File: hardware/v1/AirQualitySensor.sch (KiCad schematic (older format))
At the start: 40 parts, among them J1 USB_C_Receptacle_USB2.0, J2 SWD, J3 UART, U1 004-0-0053, U2 DHT22, U3 XC6206P332MR

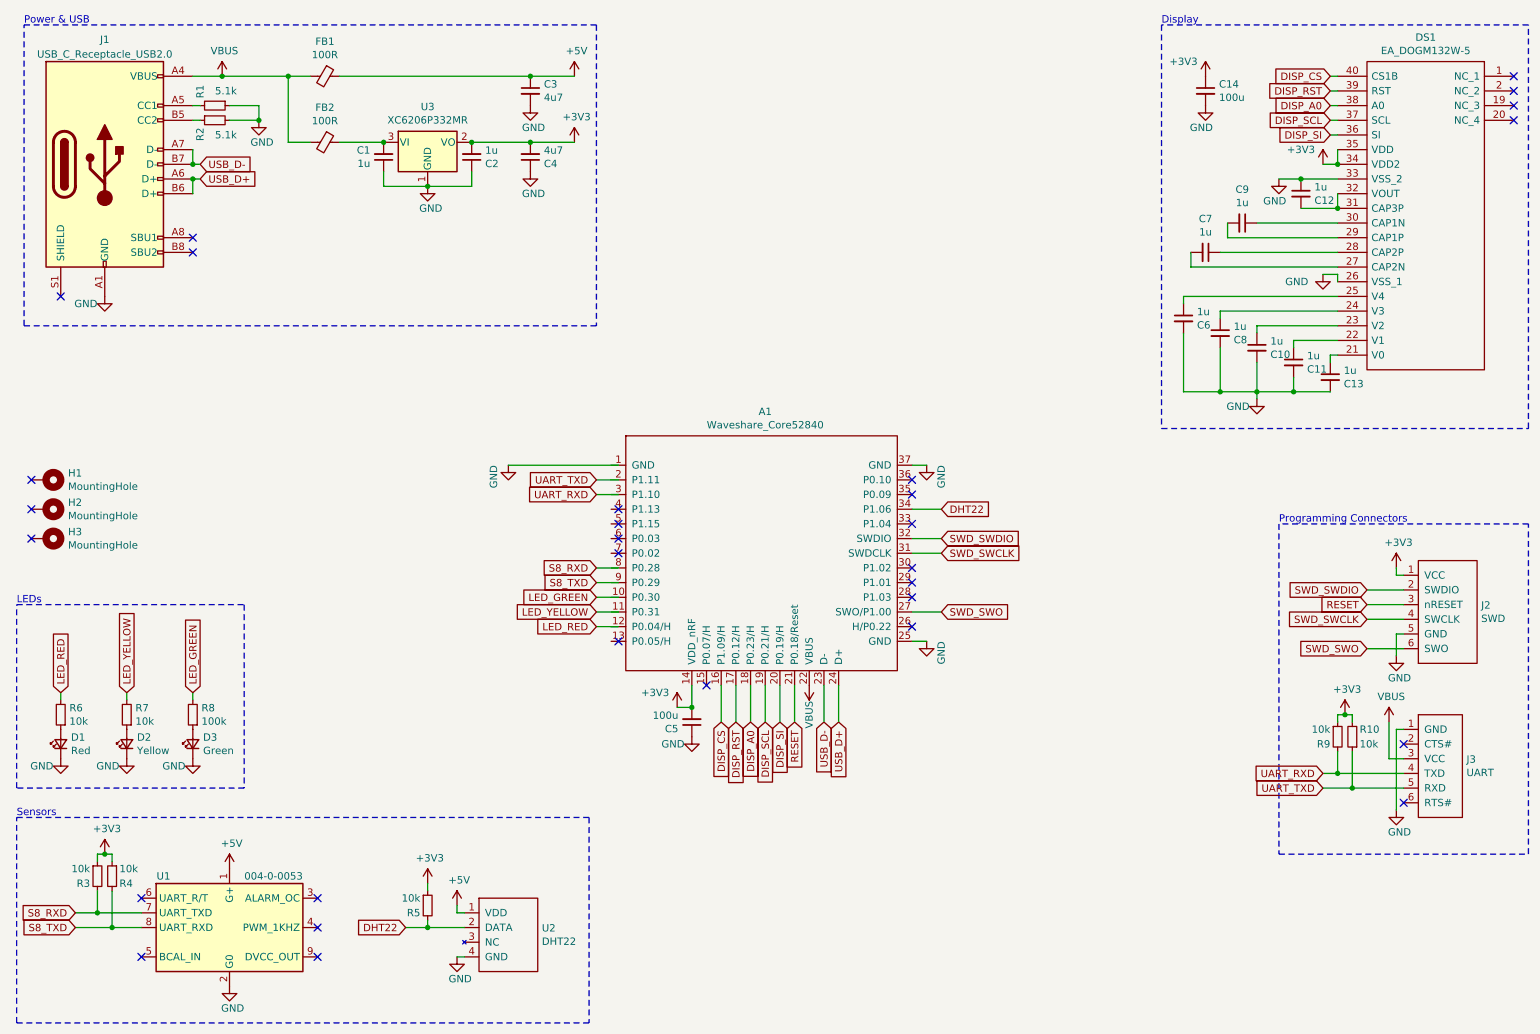
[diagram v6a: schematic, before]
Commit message: Move sensor pins to high drive output pins
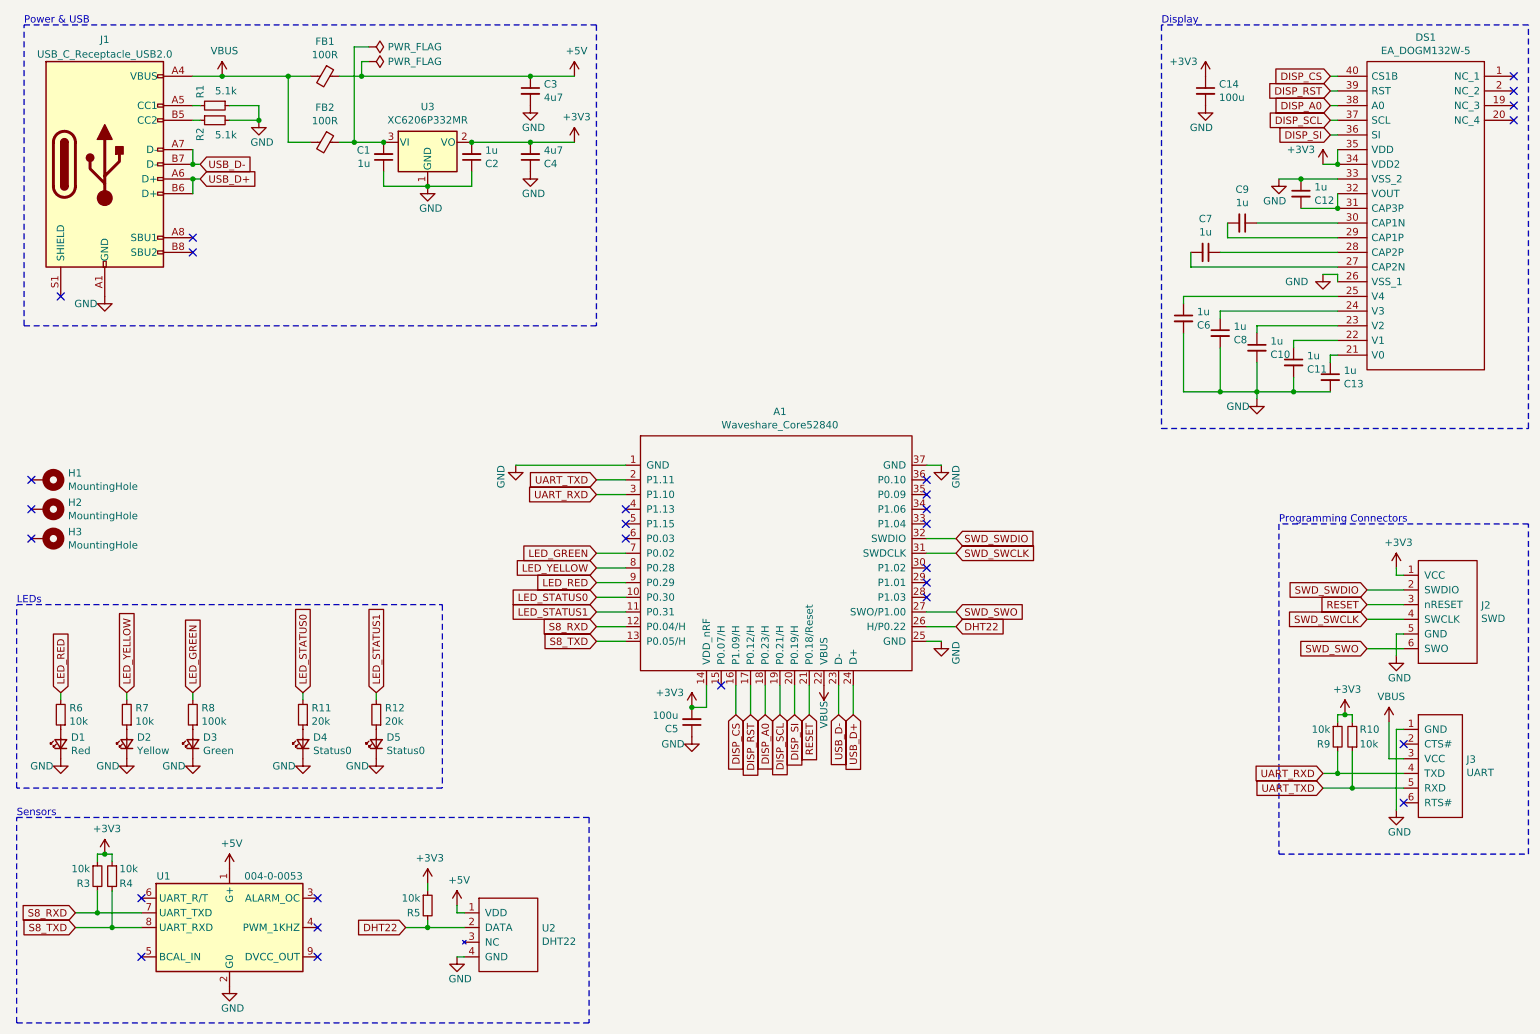
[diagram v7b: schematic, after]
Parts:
- added D4, D5: Status0, LED_SMD:LED_0805_2012Metric, symbol Device:LED_Small
- added R11, R12: 20k, Resistor_SMD:R_0402_1005Metric, symbol Device:R_Small
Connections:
- net labels added: LED_STATUS0, LED_STATUS1
- wire segments 127 -> 137
- no-connect marks 30 -> 28
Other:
- moved on the sheet: A1

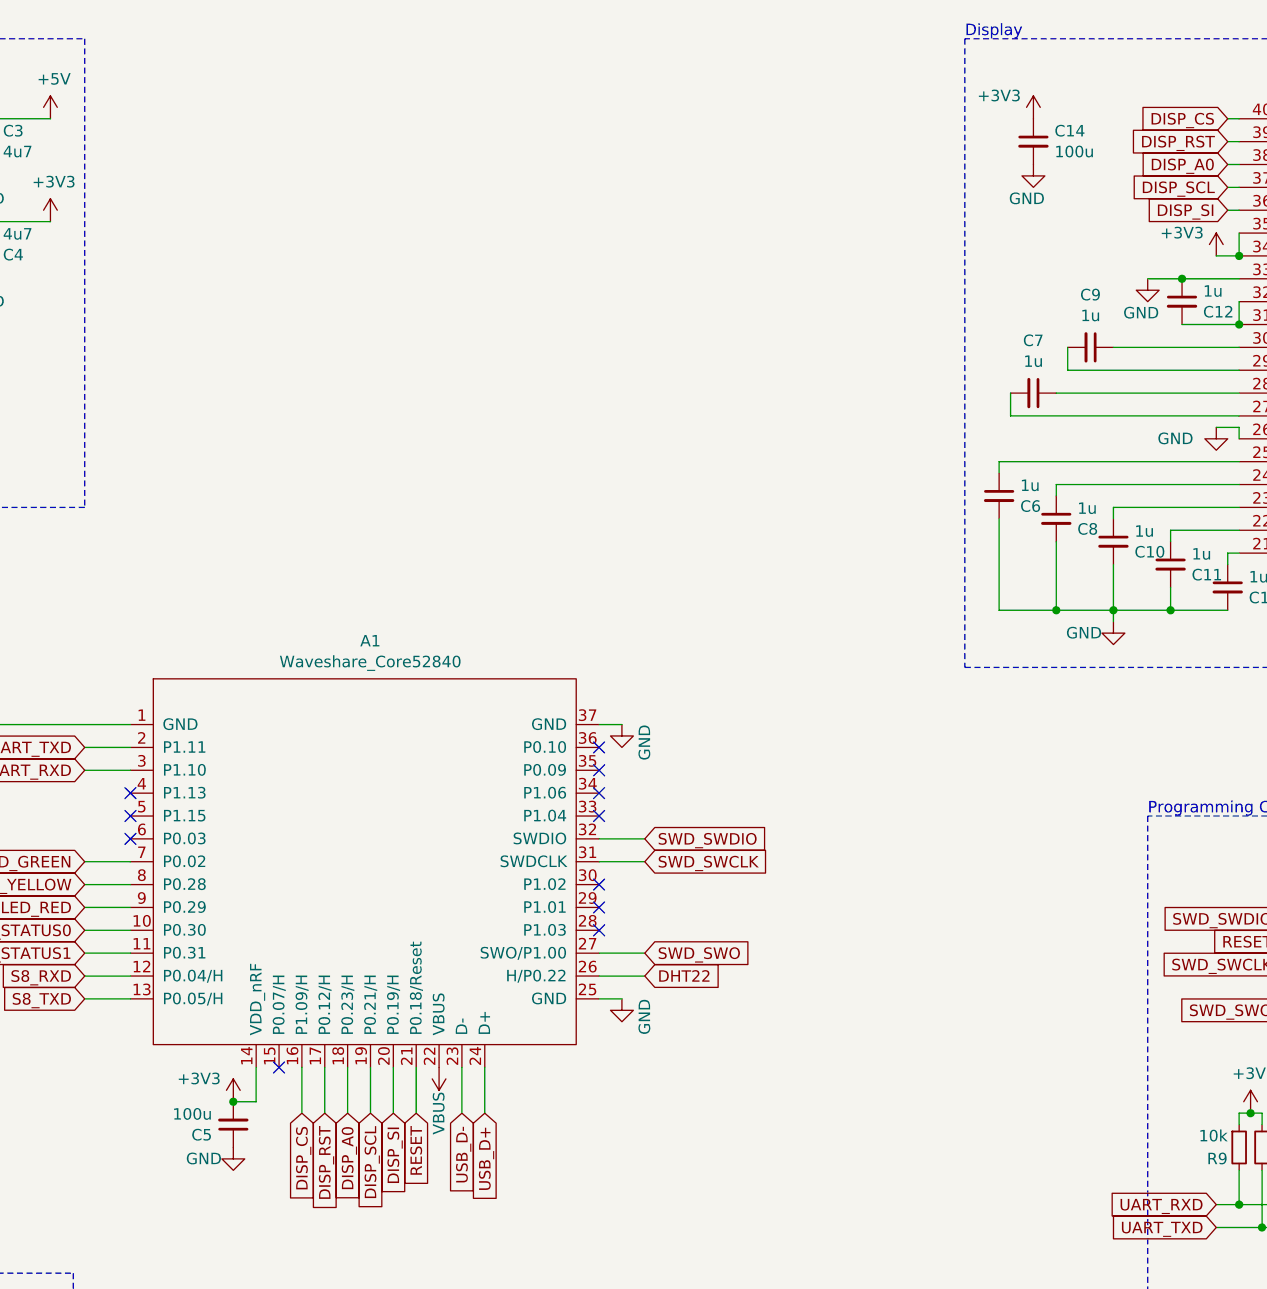
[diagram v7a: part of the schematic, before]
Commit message: Fix 100n capacitor values typo
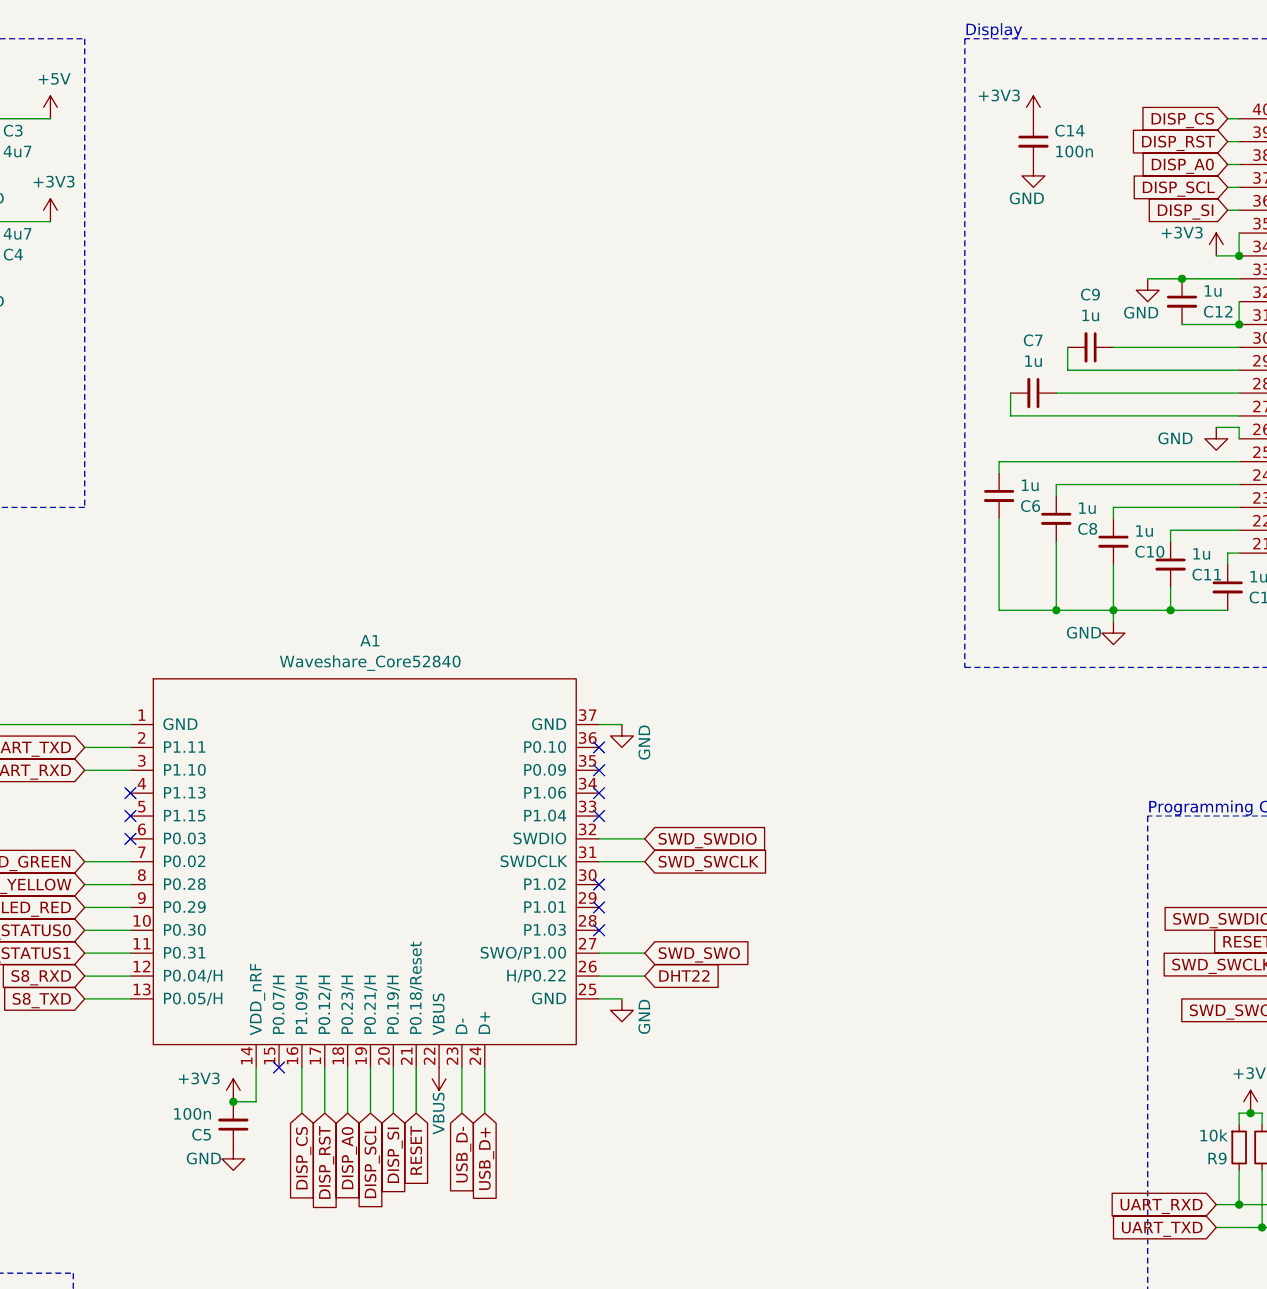
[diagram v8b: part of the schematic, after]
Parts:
- C14, C5: value 100u -> 100n
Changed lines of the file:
@@
 P 5350 5450
 F 0 "C5" H 5442 5496 50  0000 L CNN
-F 1 "100u" H 5442 5405 50  0000 L CNN
+F 1 "100n" H 5442 5405 50  0000 L CNN
 F 2 "Capacitor_SMD:C_0402_1005Metric" H 5350 5450 50  0001 C CNN
 F 3 "~" H 5350 5450 50  0001 C CNN
@@
 P 8850 1150
 F 0 "C14" H 8942 1196 50  0000 L CNN
-F 1 "100u" H 8942 1105 50  0000 L CNN
+F 1 "100n" H 8942 1105 50  0000 L CNN
 F 2 "Capacitor_SMD:C_0402_1005Metric" H 8850 1150 50  0001 C CNN
 F 3 "~" H 8850 1150 50  0001 C CNN
